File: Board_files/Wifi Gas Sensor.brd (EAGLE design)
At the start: 76.2 x 61.9 mm, 37 parts, among them IC1 7805T, J1 DCJ0202, Q1 FQN1N50CI, Q3 FQN1N50CI

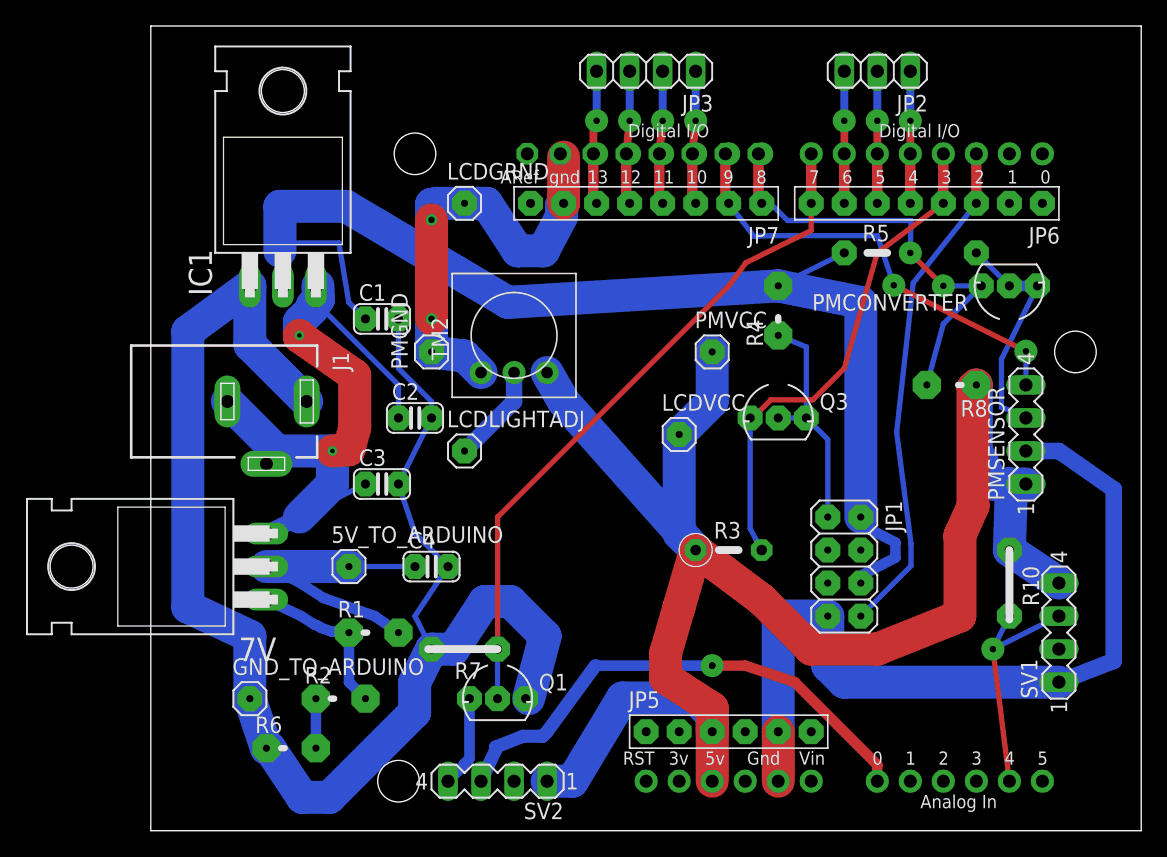
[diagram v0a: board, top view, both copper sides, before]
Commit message: corrected barrel jack routing
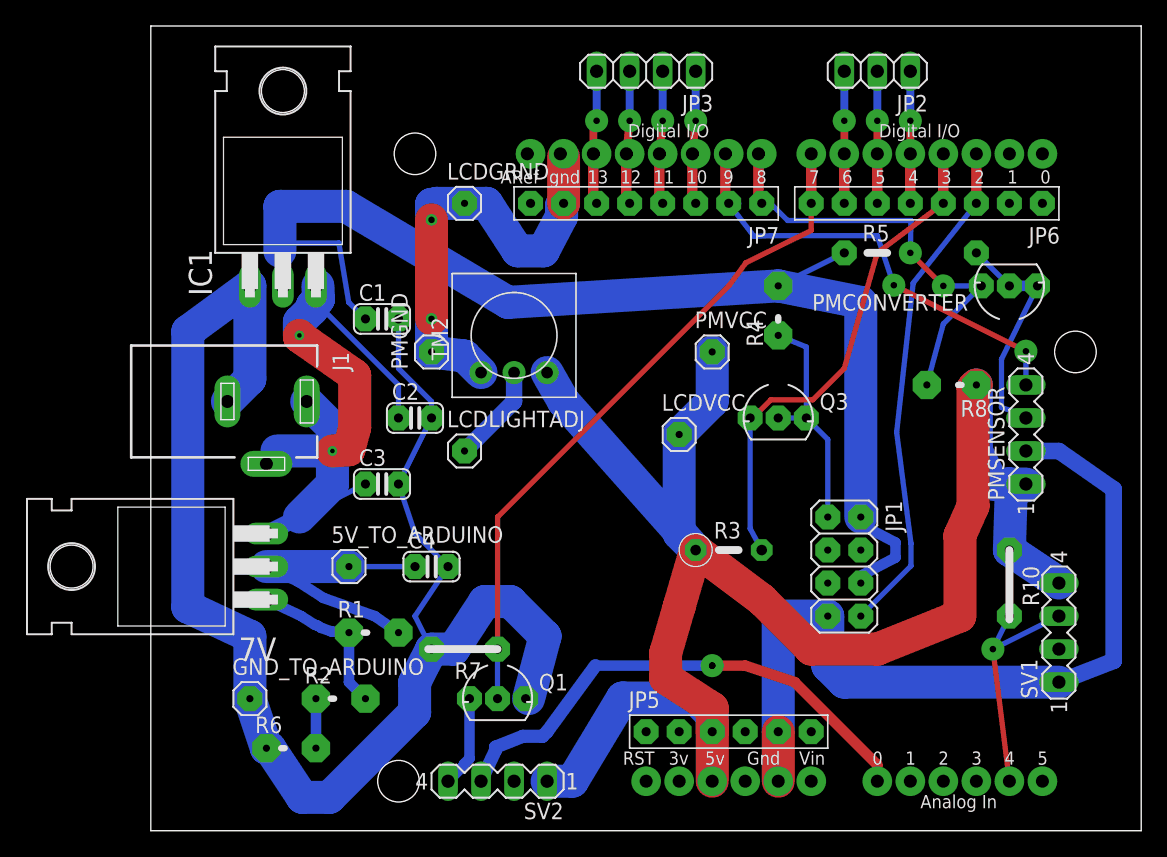
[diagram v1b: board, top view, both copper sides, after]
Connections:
- net GND_TO_ARDUINO: now also J1.3; no longer J1.1
- net N$19: now also J1.1; no longer J1.3
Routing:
- net GND_TO_ARDUINO: track 119.4 -> 118.3 mm
- net N$19: track 53.0 -> 52.2 mm
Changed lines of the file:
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@@
 <layer number="17" name="Pads" color="2" fill="1" visible="yes" active="yes"/>
 <layer number="18" name="Vias" color="2" fill="1" visible="yes" active="yes"/>
-<layer number="19" name="Unrouted" color="6" fill="1" visible="no" active="yes"/>
+<layer number="19" name="Unrouted" color="6" fill="1" visible="yes" active="yes"/>
 <layer number="20" name="Dimension" color="24" fill="1" visible="no" active="yes"/>
 <layer number="21" name="tPlace" color="7" fill="1" visible="no" active="yes"/>
 <layer number="22" name="bPlace" color="7" fill="1" visible="no" active="yes"/>
-<layer number="23" name="tOrigins" color="15" fill="1" visible="no" active="yes"/>
-<layer number="24" name="bOrigins" color="15" fill="1" visible="no" active="yes"/>
+<layer number="23" name="tOrigins" color="15" fill="1" visible="yes" active="yes"/>
+<layer number="24" name="bOrigins" color="15" fill="1" visible="yes" active="yes"/>
 <layer number="25" name="tNames" color="7" fill="1" visible="no" active="yes"/>
 <layer number="26" name="bNames" color="7" fill="1" visible="no" active="yes"/>
@@
 <wire x1="7.7724" y1="39.58413125" x2="7.812753125" y2="39.62766875" width="2.54" layer="16"/>
 <wire x1="7.774115625" y1="40.645846875" x2="7.774115625" y2="40.485884375" width="0.4064" layer="16"/>
-<contactref element="J1" pad="3"/>
-<wire x1="0.81" y1="31.75" x2="4.62" y2="27.94" width="2.54" layer="16"/>
 <via x="8.89" y="27.94" extent="1-16" drill="0.35"/>
 <wire x1="10.6024" y1="29.74660625" x2="10.6024" y2="33.75339375" width="2.54" layer="1"/>
@@
 <wire x1="7.812753125" y1="39.177246875" x2="7.812753125" y2="39.62766875" width="0.4064" layer="16"/>
 <wire x1="13.97" y1="33.02" x2="7.812753125" y2="39.177246875" width="0.4064" layer="16"/>
+<contactref element="J1" pad="1"/>
+<wire x1="6.91" y1="31.75" x2="8.89" y2="29.77" width="2.54" layer="16"/>
+<wire x1="8.89" y1="29.77" x2="8.89" y2="27.94" width="2.54" layer="16"/>
 <wire x1="7.774115625" y1="40.645846875" x2="7.62" y2="40.64" width="0" layer="19" extent="16-16"/>
 </signal>
@@
 <wire x1="25.2476" y1="13.68898125" x2="23.9776" y2="8.89" width="2.54" layer="16"/>
 <contactref element="GND_TO_ARDUINO" pad="1"/>
-<contactref element="J1" pad="1"/>
 <wire x1="-2.2352" y1="15.9313375" x2="-2.2352" y2="37.1348" width="2.54" layer="16"/>
 <wire x1="-2.2352" y1="37.1348" x2="2.54" y2="40.64" width="2.54" layer="16"/>
-<wire x1="2.54" y1="40.64" x2="2.54" y2="36.12" width="2.54" layer="16"/>
-<wire x1="2.54" y1="36.12" x2="6.91" y2="31.75" width="2.54" layer="16"/>
 <wire x1="13.97" y1="38.1" x2="13.97" y2="34.29" width="0.4064" layer="16"/>
 <wire x1="16.51" y1="31.75" x2="16.51" y2="30.48" width="0.4064" layer="16"/>
 <wire x1="13.97" y1="34.29" x2="16.51" y2="31.75" width="0.4064" layer="16"/>
+<contactref element="J1" pad="3"/>
+<wire x1="0.81" y1="31.75" x2="2.54" y2="33.48" width="2.54" layer="16"/>
+<wire x1="2.54" y1="33.48" x2="2.54" y2="40.64" width="2.54" layer="16"/>
 <wire x1="23.9776" y1="8.89" x2="23.749" y2="8.89" width="0" layer="19" extent="16-16"/>
 </signal>
@@
 </signal>
 <signal name="N$46">
-<via x="63.5" y="50.8" extent="1-16" drill="0.5" diameter="1.778"/>
+<via x="63.5" y="50.8" extent="1-16" drill="0.5" diameter="2.032"/>
 </signal>
 <signal name="N$47">
@@
 <via x="33.02" y="2.54" extent="1-16" drill="0.5" diameter="1.778"/>
 </signal>
+<signal name="N$72">
+<via x="60.96" y="50.8" extent="1-16" drill="0.5" diameter="2.032"/>
+</signal>
+<signal name="N$73">
+<via x="58.42" y="50.8" extent="1-16" drill="0.5" diameter="2.032"/>
+</signal>
+<signal name="N$74">
+<via x="55.88" y="50.8" extent="1-16" drill="0.5" diameter="2.032"/>
+</signal>
+<signal name="N$75">
+<via x="53.34" y="50.8" extent="1-16" drill="0.5" diameter="2.032"/>
+</signal>
+<signal name="N$76">
+<via x="50.8" y="50.8" extent="1-16" drill="0.5" diameter="2.032"/>
+</signal>
+<signal name="N$77">
+<via x="48.26" y="50.8" extent="1-16" drill="0.5" diameter="2.032"/>
+</signal>
+<signal name="N$78">
+<via x="45.72" y="50.8" extent="1-16" drill="0.5" diameter="2.032"/>
+</signal>
+<signal name="N$79">
+<via x="41.91" y="50.8" extent="1-16" drill="0.5" diameter="2.032"/>
+</signal>
+<signal name="N$80">
+<via x="39.37" y="50.8" extent="1-16" drill="0.5" diameter="2.032"/>
+</signal>
+<signal name="N$81">
+<via x="36.83" y="50.8" extent="1-16" drill="0.5" diameter="2.032"/>
+</signal>
+<signal name="N$82">
+<via x="34.29" y="50.8" extent="1-16" drill="0.5" diameter="2.032"/>
+</signal>
+<signal name="N$83">
+<via x="31.75" y="50.8" extent="1-16" drill="0.5" diameter="2.032"/>
+</signal>
+<signal name="N$84">
+<via x="29.21" y="50.8" extent="1-16" drill="0.5" diameter="2.032"/>
+</signal>
+<signal name="N$85">
+<via x="63.5" y="2.54" extent="1-16" drill="0.5" diameter="2.032"/>
+</signal>
+<signal name="N$86">
+<via x="60.96" y="2.54" extent="1-16" drill="0.5" diameter="2.032"/>
+</signal>
+<signal name="N$87">
+<via x="58.42" y="2.54" extent="1-16" drill="0.5" diameter="2.032"/>
+</signal>
+<signal name="N$88">
+<via x="55.88" y="2.54" extent="1-16" drill="0.5" diameter="2.032"/>
+</signal>
+<signal name="N$89">
+<via x="53.34" y="2.54" extent="1-16" drill="0.5" diameter="2.286"/>
+</signal>
+<signal name="N$90">
+<via x="50.8" y="2.54" extent="1-16" drill="0.5" diameter="2.032"/>
+</signal>
+<signal name="N$91">
+<via x="55.88" y="2.54" extent="1-16" drill="0.5" diameter="2.286"/>
+</signal>
+<signal name="N$92">
+<via x="58.42" y="2.54" extent="1-16" drill="0.5" diameter="2.286"/>
+</signal>
+<signal name="N$93">
+<via x="60.96" y="2.54" extent="1-16" drill="0.5" diameter="2.286"/>
+</signal>
+<signal name="N$94">
+<via x="63.5" y="2.54" extent="1-16" drill="0.5" diameter="2.286"/>
+</signal>
+<signal name="N$95">
+<via x="50.8" y="2.54" extent="1-16" drill="0.5" diameter="2.286"/>
+</signal>
+<signal name="N$96">
+<via x="45.72" y="2.54" extent="1-16" drill="0.5" diameter="2.286"/>
+</signal>
+<signal name="N$97">
+<via x="43.18" y="2.54" extent="1-16" drill="0.5" diameter="2.286"/>
+</signal>
+<signal name="N$98">
+<via x="40.64" y="2.54" extent="1-16" drill="0.5" diameter="2.286"/>
+</signal>
+<signal name="N$99">
+<via x="35.56" y="2.54" extent="1-16" drill="0.5" diameter="2.286"/>
+</signal>
+<signal name="N$100">
+<via x="38.1" y="2.54" extent="1-16" drill="0.5" diameter="2.286"/>
+</signal>
+<signal name="N$101">
+<via x="33.02" y="2.54" extent="1-16" drill="0.5" diameter="2.286"/>
+</signal>
+<signal name="N$102">
+<via x="63.5" y="50.8" extent="1-16" drill="0.5" diameter="2.286"/>
+</signal>
+<signal name="N$103">
+<via x="60.96" y="50.8" extent="1-16" drill="0.5" diameter="2.286"/>
+</signal>
+<signal name="N$104">
+<via x="58.42" y="50.8" extent="1-16" drill="0.5" diameter="2.286"/>
+</signal>
+<signal name="N$105">
+<via x="55.88" y="50.8" extent="1-16" drill="0.5" diameter="2.286"/>
+</signal>
+<signal name="N$106">
+<via x="53.34" y="50.8" extent="1-16" drill="0.5" diameter="2.286"/>
+</signal>
+<signal name="N$107">
+<via x="50.8" y="50.8" extent="1-16" drill="0.5" diameter="2.286"/>
+</signal>
+<signal name="N$108">
+<via x="48.26" y="50.8" extent="1-16" drill="0.5" diameter="2.286"/>
+</signal>
+<signal name="N$109">
+<via x="45.72" y="50.8" extent="1-16" drill="0.5" diameter="2.286"/>
+</signal>
+<signal name="N$110">
+<via x="41.91" y="50.8" extent="1-16" drill="0.5" diameter="2.286"/>
+</signal>
+<signal name="N$111">
+<via x="39.37" y="50.8" extent="1-16" drill="0.5" diameter="2.286"/>
+</signal>
+<signal name="N$112">
+<via x="36.83" y="50.8" extent="1-16" drill="0.5" diameter="2.286"/>
+</signal>
+<signal name="N$113">
+<via x="34.29" y="50.8" extent="1-16" drill="0.5" diameter="2.286"/>
+</signal>
+<signal name="N$114">
+<via x="31.75" y="50.8" extent="1-16" drill="0.5" diameter="2.286"/>
+</signal>
+<signal name="N$115">
+<via x="29.21" y="50.8" extent="1-16" drill="0.5" diameter="2.286"/>
+</signal>
+<signal name="N$116">
+<via x="26.67" y="50.8" extent="1-16" drill="0.5" diameter="2.286"/>
+</signal>
+<signal name="N$117">
+<via x="24.13" y="50.8" extent="1-16" drill="0.5" diameter="2.286"/>
+</signal>
 </signals>
